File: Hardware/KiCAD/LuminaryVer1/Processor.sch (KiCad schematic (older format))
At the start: 16 parts, among them SW1 SW_Push, U2 STM32L432KBUx, U6 AT25SF081-SSHD-X

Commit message: Routed entire power section
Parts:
- added D10: GLED, Diode_SMD:D_0603_1608Metric, symbol Device:LED
- added R32: 10k, Resistor_SMD:R_0402_1005Metric, symbol Device:R_US
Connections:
- net GND: now also D10.1 (K)
- net StatusLED: now reaches U2.2 (PC14)
- net StatusLED: now also R32.2
- new net: D10.2 (A), R32.1
- no-connect marks 1 -> 0
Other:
- note added: "This LED is driven by a very low current source (PC14) and cannot \nexceed 3mA. See RM0394 for details."
- moved on the sheet: C1, C2, C3, C4, R1, R11, R13, R2, R3, R4, R5, R6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

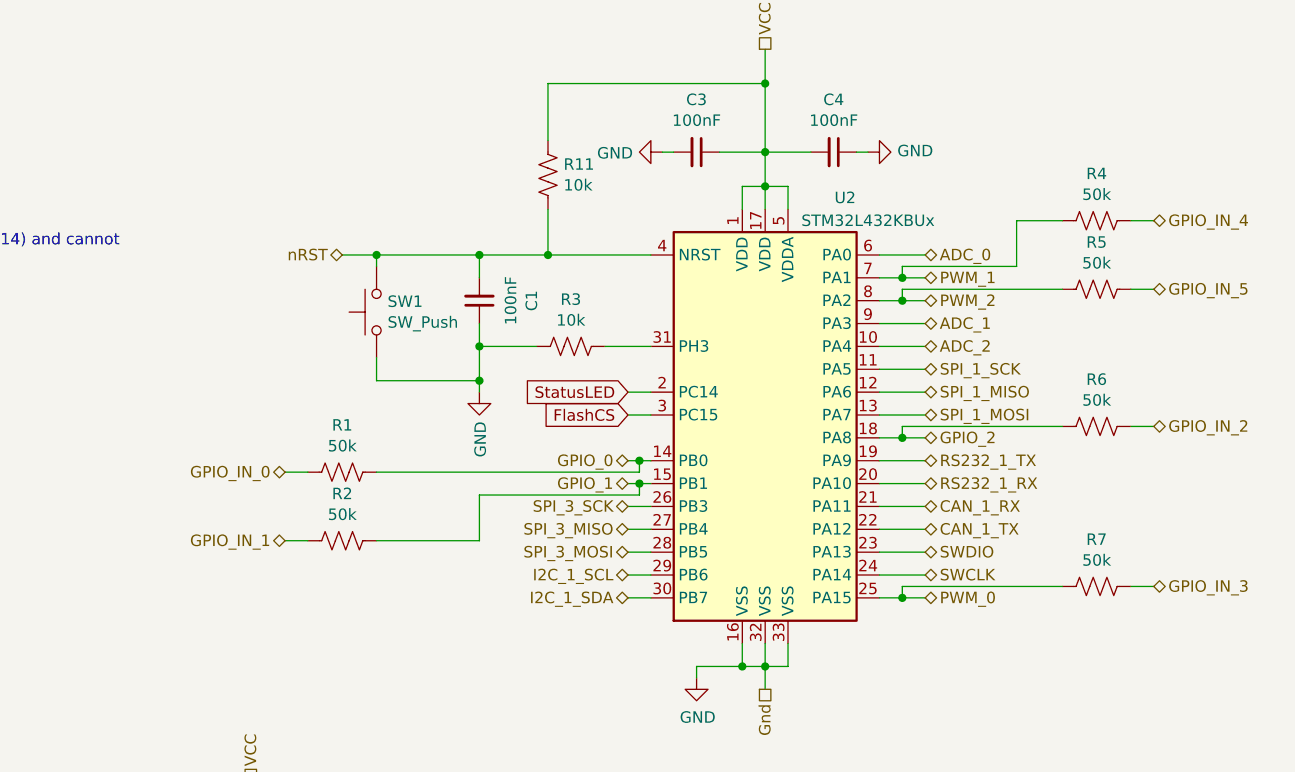
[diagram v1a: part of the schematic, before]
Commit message: Added majority of the logic level circuitry. Almost done routing connections.
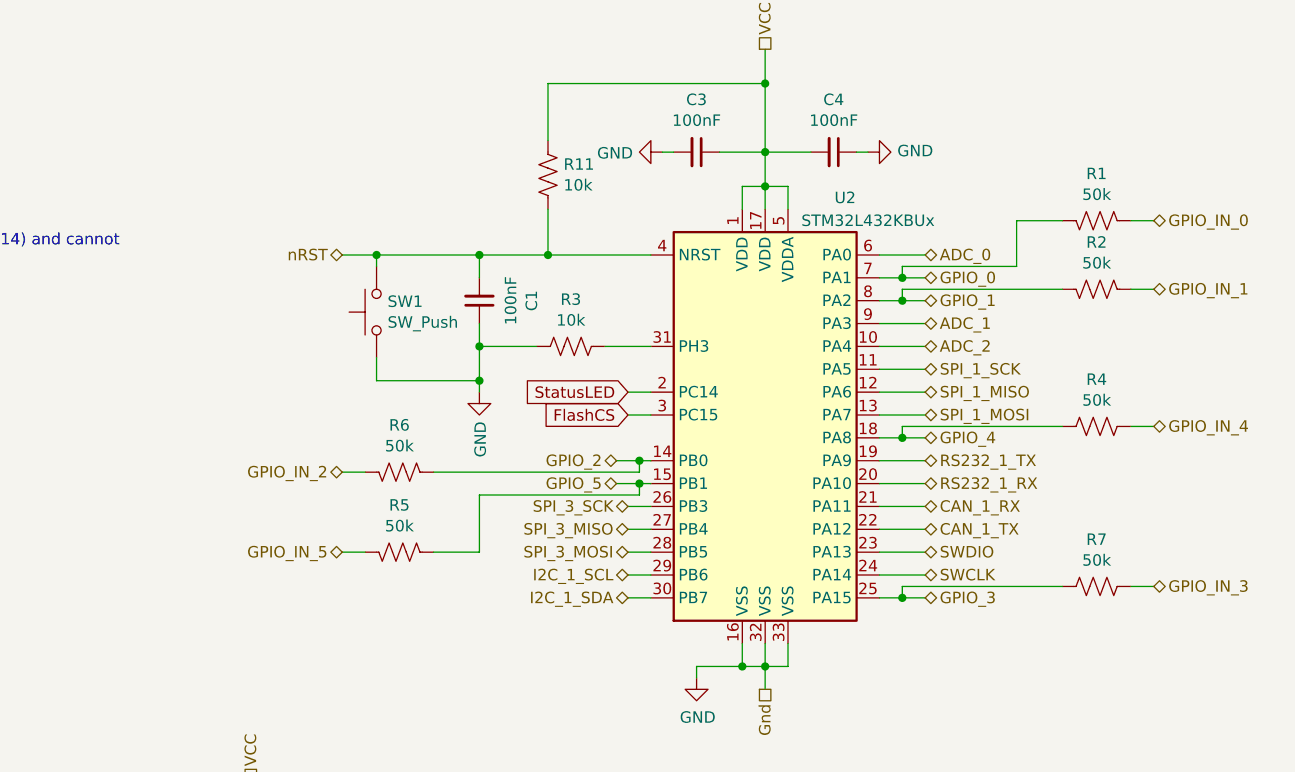
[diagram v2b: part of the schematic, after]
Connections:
- net GPIO_0: now also U2.7 (PA1); no longer U2.14 (PB0)
- net GPIO_1: now also U2.8 (PA2); no longer U2.15 (PB1)
- net GPIO_2: now also U2.14 (PB0); no longer U2.18 (PA8)
- net PWM_0 renamed GPIO_3
- net PWM_1 renamed GPIO_4
- net GPIO_4: now also U2.18 (PA8); no longer U2.7 (PA1)
- net PWM_2 renamed GPIO_5
- net GPIO_5: now also U2.15 (PB1); no longer U2.8 (PA2)
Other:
- moved on the sheet: R1, R2, R4, R5, R6
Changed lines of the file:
@@
 Text HLabel 6150 2950 0    50   BiDi ~ 0
 SPI_3_SCK
-Text HLabel 6150 2750 0    50   BiDi ~ 0
+Text HLabel 7450 1950 2    50   BiDi ~ 0
 GPIO_0
-Text HLabel 6150 2850 0    50   BiDi ~ 0
+Text HLabel 7450 2050 2    50   BiDi ~ 0
 GPIO_1
-Wire Wire Line
-	6150 2850 6200 2850
-Wire Wire Line
-	6150 2750 6200 2750
 Wire Wire Line
 	7450 3350 7350 3350
 Text HLabel 7450 3350 2    50   BiDi ~ 0
-PWM_0
+GPIO_3
 Text HLabel 7450 3050 2    50   BiDi ~ 0
 CAN_1_TX
@@
 Text HLabel 7450 2850 2    50   BiDi ~ 0
 RS232_1_RX
-Text HLabel 7450 2650 2    50   BiDi ~ 0
+Text HLabel 6100 2750 0    50   BiDi ~ 0
 GPIO_2
 Wire Wire Line
@@
 Text HLabel 7450 1850 2    50   BiDi ~ 0
 ADC_0
-Text HLabel 7450 1950 2    50   BiDi ~ 0
-PWM_1
-Text HLabel 7450 2050 2    50   BiDi ~ 0
-PWM_2
+Text HLabel 7450 2650 2    50   BiDi ~ 0
+GPIO_4
+Text HLabel 6100 2850 0    50   BiDi ~ 0
+GPIO_5
 Wire Wire Line
 	7250 3150 7450 3150
@@
 Wire Wire Line
 	6150 3350 6250 3350
-Text HLabel 4650 2800 0    50   BiDi ~ 0
+Text HLabel 8450 1700 2    50   BiDi ~ 0
 GPIO_IN_0
-Text HLabel 4650 3100 0    50   BiDi ~ 0
+Text HLabel 8450 2000 2    50   BiDi ~ 0
 GPIO_IN_1
-Text HLabel 8450 2600 2    50   BiDi ~ 0
+Text HLabel 4900 2800 0    50   BiDi ~ 0
 GPIO_IN_2
 Text HLabel 8450 3300 2    50   BiDi ~ 0
 GPIO_IN_3
-Text HLabel 8450 1700 2    50   BiDi ~ 0
+Text HLabel 8450 2600 2    50   BiDi ~ 0
 GPIO_IN_4
-Text HLabel 8450 2000 2    50   BiDi ~ 0
+Text HLabel 4900 3150 0    50   BiDi ~ 0
 GPIO_IN_5
 Wire Wire Line
@@
 	6200 2750 6250 2750
 Wire Wire Line
-	5500 2900 6200 2900
-Wire Wire Line
 	6200 2900 6200 2850
 Connection ~ 6200 2850
@@
 L Device:R_US R1
 U 1 1 5E67EEA7
-P 4900 2800
-F 0 "R1" V 5105 2800 50  0000 C CNN
-F 1 "50k" V 5014 2800 50  0000 C CNN
-F 2 "Resistor_SMD:R_0402_1005Metric" V 4940 2790 50  0001 C CNN
-F 3 "~" H 4900 2800 50  0001 C CNN
-	1    4900 2800
-	0    -1   -1   0
+P 8200 1700
+F 0 "R1" V 8405 1700 50  0000 C CNN
+F 1 "50k" V 8314 1700 50  0000 C CNN
+F 2 "Resistor_SMD:R_0402_1005Metric" V 8240 1690 50  0001 C CNN
+F 3 "~" H 8200 1700 50  0001 C CNN
+	1    8200 1700
+	0    1    -1   0
 $EndComp
 $Comp
 L Device:R_US R2
 U 1 1 5E67F864
-P 4900 3100
-F 0 "R2" V 4695 3100 50  0000 C CNN
-F 1 "50k" V 4786 3100 50  0000 C CNN
-F 2 "Resistor_SMD:R_0402_1005Metric" V 4940 3090 50  0001 C CNN
-F 3 "~" H 4900 3100 50  0001 C CNN
-	1    4900 3100
-	0    1    1    0
-$EndComp
-Wire Wire Line
-	5050 3100 5500 3100
-Wire Wire Line
-	5500 2900 5500 3100
-Wire Wire Line
-	4650 2800 4750 2800
-Wire Wire Line
-	4650 3100 4750 3100
+P 8200 2000
+F 0 "R2" V 7995 2000 50  0000 C CNN
+F 1 "50k" V 8086 2000 50  0000 C CNN
+F 2 "Resistor_SMD:R_0402_1005Metric" V 8240 1990 50  0001 C CNN
+F 3 "~" H 8200 2000 50  0001 C CNN
+	1    8200 2000
+	0    -1   1    0
+$EndComp
+Wire Wire Line
+	8450 1700 8350 1700
+Wire Wire Line
+	8450 2000 8350 2000
 $Comp
 L Device:R_US R6
 U 1 1 5E68A214
-P 8200 2600
-F 0 "R6" V 8405 2600 50  0000 C CNN
-F 1 "50k" V 8314 2600 50  0000 C CNN
-F 2 "Resistor_SMD:R_0402_1005Metric" V 8240 2590 50  0001 C CNN
-F 3 "~" H 8200 2600 50  0001 C CNN
-	1    8200 2600
-	0    -1   -1   0
+P 5150 2800
+F 0 "R6" V 5355 2800 50  0000 C CNN
+F 1 "50k" V 5264 2800 50  0000 C CNN
+F 2 "Resistor_SMD:R_0402_1005Metric" V 5190 2790 50  0001 C CNN
+F 3 "~" H 5150 2800 50  0001 C CNN
+	1    5150 2800
+	0    1    -1   0
 $EndComp
 $Comp
@@
 L Device:R_US R4
 U 1 1 5E68B831
-P 8200 1700
-F 0 "R4" V 8405 1700 50  0000 C CNN
-F 1 "50k" V 8314 1700 50  0000 C CNN
-F 2 "Resistor_SMD:R_0402_1005Metric" V 8240 1690 50  0001 C CNN
-F 3 "~" H 8200 1700 50  0001 C CNN
-	1    8200 1700
+P 8200 2600
+F 0 "R4" V 8405 2600 50  0000 C CNN
+F 1 "50k" V 8314 2600 50  0000 C CNN
+F 2 "Resistor_SMD:R_0402_1005Metric" V 8240 2590 50  0001 C CNN
+F 3 "~" H 8200 2600 50  0001 C CNN
+	1    8200 2600
 	0    -1   -1   0
 $EndComp
@@
 L Device:R_US R5
 U 1 1 5E68CD5A
-P 8200 2000
-F 0 "R5" V 8405 2000 50  0000 C CNN
-F 1 "50k" V 8314 2000 50  0000 C CNN
-F 2 "Resistor_SMD:R_0402_1005Metric" V 8240 1990 50  0001 C CNN
-F 3 "~" H 8200 2000 50  0001 C CNN
-	1    8200 2000
-	0    -1   -1   0
+P 5150 3150
+F 0 "R5" V 5355 3150 50  0000 C CNN
+F 1 "50k" V 5264 3150 50  0000 C CNN
+F 2 "Resistor_SMD:R_0402_1005Metric" V 5190 3140 50  0001 C CNN
+F 3 "~" H 5150 3150 50  0001 C CNN
+	1    5150 3150
+	0    1    -1   0
 $EndComp
 Wire Wire Line
@@
 	7850 1900 7350 1900
 Wire Wire Line
-	8350 1700 8450 1700
-Wire Wire Line
-	8350 2000 8450 2000
-Wire Wire Line
 	8350 2600 8450 2600
+Wire Wire Line
+	5000 3150 4900 3150
+Wire Wire Line
+	5000 2800 4900 2800
 Wire Wire Line
 	8350 3300 8450 3300
@@
 	6750 950  6750 1100
 Connection ~ 6750 1100
-Wire Wire Line
-	5050 2800 6200 2800
 $Comp
 L Switch:SW_Push SW1
@@
 Wire Wire Line
 	4500 5650 4500 5750
-Text HLabel 3500 5050 0    50   BiDi ~ 0
-SPI_1_SCK
-Text HLabel 5200 4950 2    50   BiDi ~ 0
-SPI_1_MISO
-Text HLabel 3500 4950 0    50   BiDi ~ 0
-SPI_1_MOSI
 Wire Wire Line
 	3900 5250 3700 5250
@@
 Wire Wire Line
 	3700 5250 3700 5350
-Wire Wire Line
-	5100 4950 5200 4950
-Wire Wire Line
-	3500 4950 3900 4950
-Wire Wire Line
-	3500 5050 3900 5050
-Wire Wire Line
-	3500 5150 3900 5150
 Text GLabel 6150 2550 0    50   Input ~ 0
-FlashCS
-Text GLabel 3500 5150 0    50   Input ~ 0
 FlashCS
 Wire Wire Line
@@
 Text Notes 1650 1900 0    50   ~ 0
 This LED is driven by a very low current source (PC14) and cannot \nexceed 3mA. See RM0394 for details.
+Wire Wire Line
+	5500 3150 5500 2900
+Wire Wire Line
+	5500 2900 6200 2900
+Wire Wire Line
+	6100 2750 6200 2750
+Wire Wire Line
+	5300 2800 6200 2800
+Wire Wire Line
+	5500 3150 5300 3150
+Wire Wire Line
+	6100 2850 6200 2850
+Wire Wire Line
+	5100 4950 5200 4950
+Text HLabel 5200 4950 2    50   BiDi ~ 0
+SPI_1_MISO
+Wire Wire Line
+	3500 5050 3900 5050
+Wire Wire Line
+	3500 5150 3900 5150
+Text GLabel 3500 5150 0    50   Input ~ 0
+FlashCS
+Text HLabel 3500 5050 0    50   BiDi ~ 0
+SPI_1_SCK
+Text HLabel 3500 4950 0    50   BiDi ~ 0
+SPI_1_MOSI
+Wire Wire Line
+	3500 4950 3900 4950
 $EndSCHEMATC

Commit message: Finalized for version 1 production.
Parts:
- C1, C2, C3, C4: LCSC (none) -> C1525; PartNumber (none) -> CL05B104KO5NNNC
- D10: LCSC (none) -> C205443; PartNumber (none) -> ORH-G36G
- R1, R2, R4, R5, R6, R7: value 50k -> 47k; LCSC (none) -> C25792; PartNumber (none) -> 0402WGF4702TCE
- R11, R3, R32: LCSC (none) -> C102759; PartNumber (none) -> RTT02103JTH
- SW1: LCSC (none) -> C255808; PartNumber (none) -> 1TS003B-1600-3500A-CT
- U2: LCSC (none) -> C94784; PartNumber (none) -> STM32L432KBU6
- U6: LCSC (none) -> C169368; PartNumber (none) -> AT25SF081-SSHD-B
- renumbered R13 to R_PWR_3
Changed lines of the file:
@@
 F 2 "Package_DFN_QFN:QFN-32-1EP_5x5mm_P0.5mm_EP3.45x3.45mm" H 6350 1650 50  0001 R CNN
 F 3 "http://www.st.com/st-web-ui/static/active/en/resource/technical/document/datasheet/DM00257205.pdf" H 6750 2550 50  0001 C CNN
+F 4 "C94784" H 6750 2550 50  0001 C CNN "LCSC"
+F 5 "STM32L432KBU6" H 6750 2550 50  0001 C CNN "PartNumber"
 	1    6750 2550
 	1    0    0    -1
@@
 F 2 "Capacitor_SMD:C_0402_1005Metric" H 6450 1400 50  0001 C CNN
 F 3 "~" H 6450 1400 50  0001 C CNN
+F 4 "C1525" H 6450 1400 50  0001 C CNN "LCSC"
+F 5 "CL05B104KO5NNNC" H 6450 1400 50  0001 C CNN "PartNumber"
 	1    6450 1400
 	0    1    1    0
@@
 F 2 "Capacitor_SMD:C_0402_1005Metric" H 7050 1400 50  0001 C CNN
 F 3 "~" H 7050 1400 50  0001 C CNN
+F 4 "C1525" H 7050 1400 50  0001 C CNN "LCSC"
+F 5 "CL05B104KO5NNNC" H 7050 1400 50  0001 C CNN "PartNumber"
 	1    7050 1400
 	0    1    1    0
@@
 F 2 "Resistor_SMD:R_0402_1005Metric" V 5940 2240 50  0001 C CNN
 F 3 "~" H 5900 2250 50  0001 C CNN
+F 4 "C102759" H 5900 2250 50  0001 C CNN "LCSC"
+F 5 "RTT02103JTH" H 5900 2250 50  0001 C CNN "PartNumber"
 	1    5900 2250
 	0    1    1    0
@@
 P 8200 1700
 F 0 "R1" V 8405 1700 50  0000 C CNN
-F 1 "50k" V 8314 1700 50  0000 C CNN
+F 1 "47k" V 8314 1700 50  0000 C CNN
 F 2 "Resistor_SMD:R_0402_1005Metric" V 8240 1690 50  0001 C CNN
 F 3 "~" H 8200 1700 50  0001 C CNN
+F 4 "C25792" H 8200 1700 50  0001 C CNN "LCSC"
+F 5 "0402WGF4702TCE" H 8200 1700 50  0001 C CNN "PartNumber"
 	1    8200 1700
 	0    1    -1   0
@@
 P 8200 2000
 F 0 "R2" V 7995 2000 50  0000 C CNN
-F 1 "50k" V 8086 2000 50  0000 C CNN
+F 1 "47k" V 8086 2000 50  0000 C CNN
 F 2 "Resistor_SMD:R_0402_1005Metric" V 8240 1990 50  0001 C CNN
 F 3 "~" H 8200 2000 50  0001 C CNN
+F 4 "C25792" H 8200 2000 50  0001 C CNN "LCSC"
+F 5 "0402WGF4702TCE" H 8200 2000 50  0001 C CNN "PartNumber"
 	1    8200 2000
 	0    -1   1    0
@@
 P 5150 2800
 F 0 "R6" V 5355 2800 50  0000 C CNN
-F 1 "50k" V 5264 2800 50  0000 C CNN
+F 1 "47k" V 5264 2800 50  0000 C CNN
 F 2 "Resistor_SMD:R_0402_1005Metric" V 5190 2790 50  0001 C CNN
 F 3 "~" H 5150 2800 50  0001 C CNN
+F 4 "C25792" H 5150 2800 50  0001 C CNN "LCSC"
+F 5 "0402WGF4702TCE" H 5150 2800 50  0001 C CNN "PartNumber"
 	1    5150 2800
 	0    1    -1   0
@@
 P 8200 3300
 F 0 "R7" V 8405 3300 50  0000 C CNN
-F 1 "50k" V 8314 3300 50  0000 C CNN
+F 1 "47k" V 8314 3300 50  0000 C CNN
 F 2 "Resistor_SMD:R_0402_1005Metric" V 8240 3290 50  0001 C CNN
 F 3 "~" H 8200 3300 50  0001 C CNN
+F 4 "C25792" H 8200 3300 50  0001 C CNN "LCSC"
+F 5 "0402WGF4702TCE" H 8200 3300 50  0001 C CNN "PartNumber"
 	1    8200 3300
 	0    -1   -1   0
@@
 P 8200 2600
 F 0 "R4" V 8405 2600 50  0000 C CNN
-F 1 "50k" V 8314 2600 50  0000 C CNN
+F 1 "47k" V 8314 2600 50  0000 C CNN
 F 2 "Resistor_SMD:R_0402_1005Metric" V 8240 2590 50  0001 C CNN
 F 3 "~" H 8200 2600 50  0001 C CNN
+F 4 "C25792" H 8200 2600 50  0001 C CNN "LCSC"
+F 5 "0402WGF4702TCE" H 8200 2600 50  0001 C CNN "PartNumber"
 	1    8200 2600
 	0    -1   -1   0
@@
 P 5150 3150
 F 0 "R5" V 5355 3150 50  0000 C CNN
-F 1 "50k" V 5264 3150 50  0000 C CNN
+F 1 "47k" V 5264 3150 50  0000 C CNN
 F 2 "Resistor_SMD:R_0402_1005Metric" V 5190 3140 50  0001 C CNN
 F 3 "~" H 5150 3150 50  0001 C CNN
+F 4 "C25792" H 5150 3150 50  0001 C CNN "LCSC"
+F 5 "0402WGF4702TCE" H 5150 3150 50  0001 C CNN "PartNumber"
 	1    5150 3150
 	0    1    -1   0
@@
 F 2 "Resistor_SMD:R_0402_1005Metric" V 5840 1490 50  0001 C CNN
 F 3 "~" H 5800 1500 50  0001 C CNN
+F 4 "C102759" H 5800 1500 50  0001 C CNN "LCSC"
+F 5 "RTT02103JTH" H 5800 1500 50  0001 C CNN "PartNumber"
 	1    5800 1500
 	-1   0    0    1
@@
 F 2 "button:LCSC_C255808_HYP_2x4x3.5mm_RightAngle" H 5050 2300 50  0001 C CNN
 F 3 "~" H 5050 2300 50  0001 C CNN
+F 4 "C255808" H 5050 2100 50  0001 C CNN "LCSC"
+F 5 "1TS003B-1600-3500A-CT" H 5050 2100 50  0001 C CNN "PartNumber"
 	1    5050 2100
 	0    -1   -1   0
@@
 F 2 "Capacitor_SMD:C_0402_1005Metric" H 5500 2050 50  0001 C CNN
 F 3 "~" H 5500 2050 50  0001 C CNN
+F 4 "C1525" H 5500 2050 50  0001 C CNN "LCSC"
+F 5 "CL05B104KO5NNNC" H 5500 2050 50  0001 C CNN "PartNumber"
 	1    5500 2050
 	-1   0    0    1
@@
 VCC
 $Comp
-L Device:R_US R13
+L Device:R_US R_PWR_3
 U 1 1 5EB3E2A2
 P 4500 4400
-F 0 "R13" V 4705 4400 50  0000 C CNN
+F 0 "R_PWR_3" V 4705 4400 50  0000 C CNN
 F 1 "0" V 4614 4400 50  0000 C CNN
 F 2 "Resistor_SMD:R_0402_1005Metric" V 4540 4390 50  0001 C CNN
@@
 F 2 "Capacitor_SMD:C_0402_1005Metric" H 4900 4600 50  0001 C CNN
 F 3 "~" H 4900 4600 50  0001 C CNN
+F 4 "C1525" H 4900 4600 50  0001 C CNN "LCSC"
+F 5 "CL05B104KO5NNNC" H 4900 4600 50  0001 C CNN "PartNumber"
 	1    4900 4600
 	0    1    1    0
@@
 F 2 "Package_SO:SOIC-8_3.9x4.9mm_P1.27mm" H 4500 4550 50  0001 C CNN
 F 3 "https://www.adestotech.com/wp-content/uploads/DS-AT25SF081_045.pdf" H 4500 5150 50  0001 C CNN
+F 4 "C169368" H 4500 5150 50  0001 C CNN "LCSC"
+F 5 "AT25SF081-SSHD-B" H 4500 5150 50  0001 C CNN "PartNumber"
 	1    4500 5150
 	1    0    0    -1
@@
 F 2 "Resistor_SMD:R_0402_1005Metric" V 2840 2290 50  0001 C CNN
 F 3 "~" H 2800 2300 50  0001 C CNN
+F 4 "C102759" H 2800 2300 50  0001 C CNN "LCSC"
+F 5 "RTT02103JTH" H 2800 2300 50  0001 C CNN "PartNumber"
 	1    2800 2300
 	-1   0    0    1
@@
 F 2 "Diode_SMD:D_0603_1608Metric" H 2800 2700 50  0001 C CNN
 F 3 "~" H 2800 2700 50  0001 C CNN
+F 4 "C205443" H 2800 2700 50  0001 C CNN "LCSC"
+F 5 "ORH-G36G" H 2800 2700 50  0001 C CNN "PartNumber"
 	1    2800 2700
 	0    -1   -1   0
